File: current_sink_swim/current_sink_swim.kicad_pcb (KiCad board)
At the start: 2 copper layers, 22 parts, among them J1 Conn_01x02_Socket, J2 Conn_01x03_Socket, J3 Conn_01x02_Socket, Q1 BUK9575, U1 LMV358, U3 TC1016

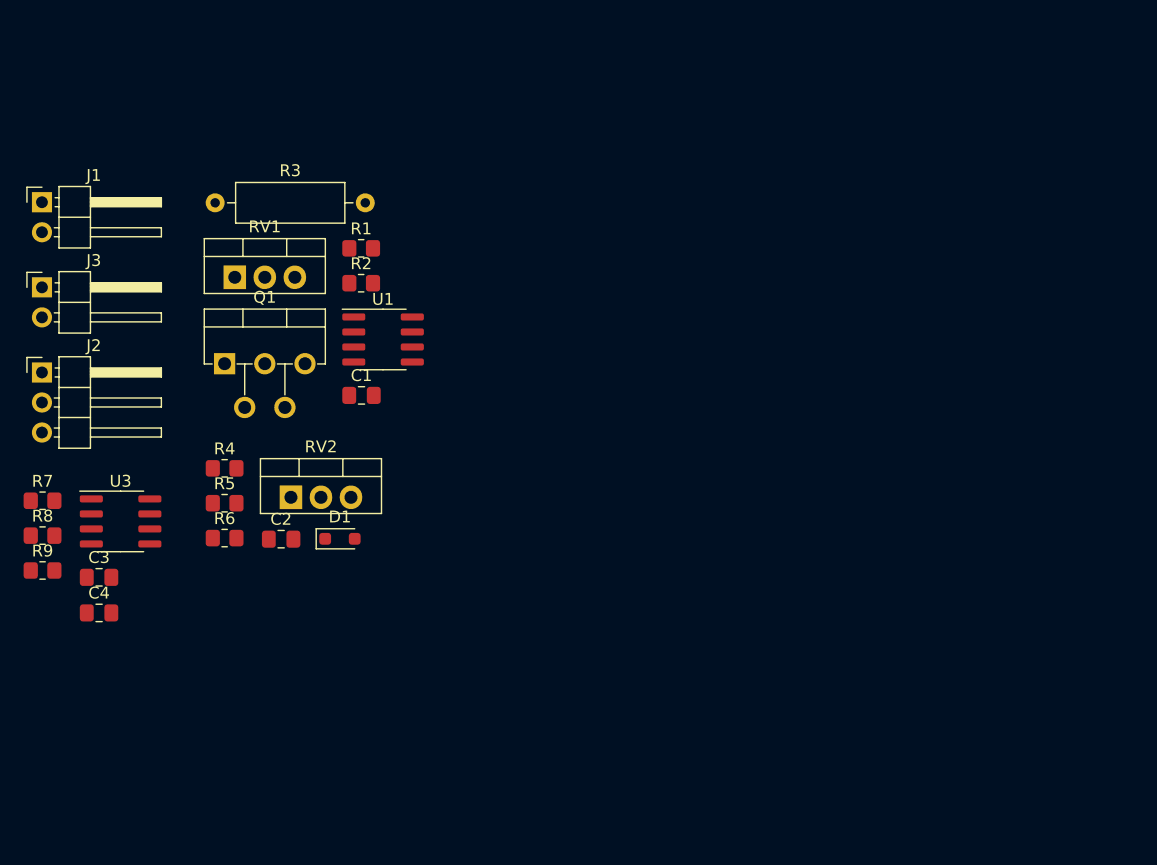
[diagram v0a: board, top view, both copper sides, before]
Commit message: created a rough board outline
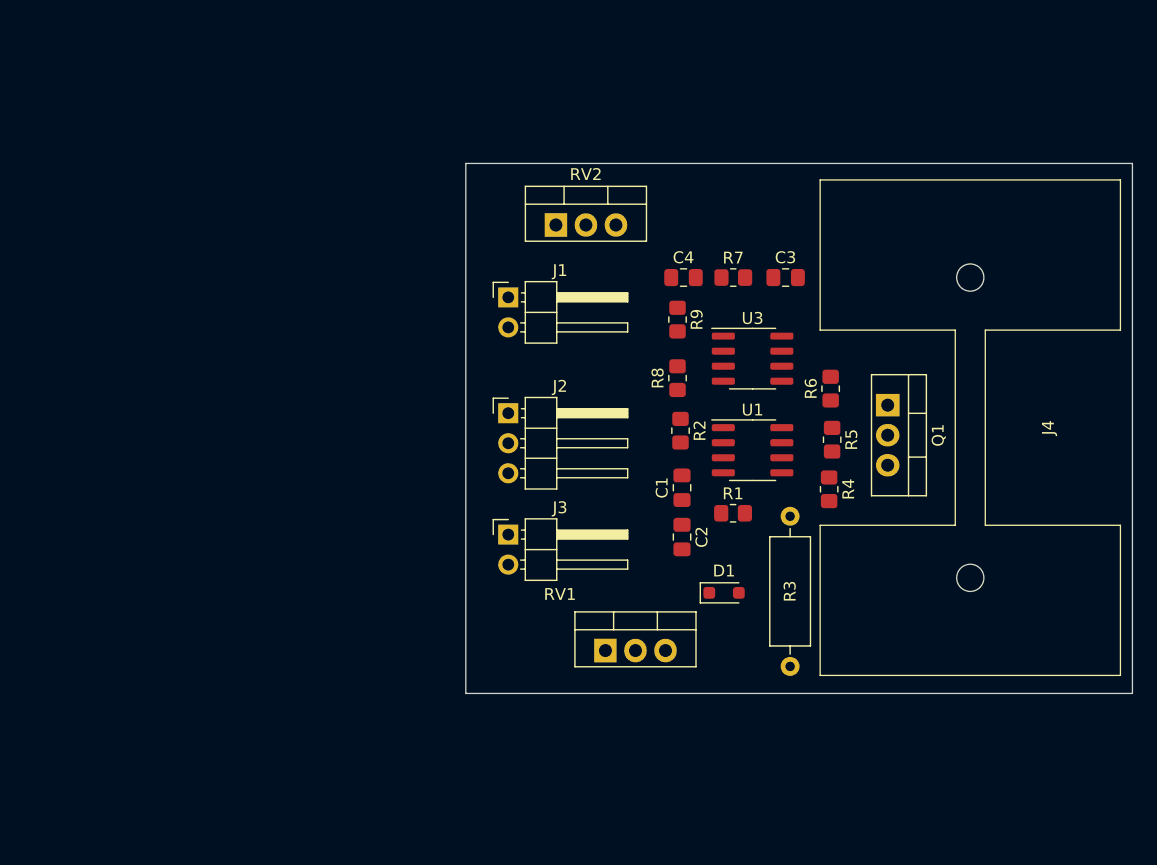
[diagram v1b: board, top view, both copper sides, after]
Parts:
- added J4: Conn_01x01_Pin, custom_modules:FAT-220, F.Cu at (142.5, 50.2)
- Q1: value BUK9575 -> IRF530NPBF; footprint Package_TO_SOT_THT:TO-220-5_P3.4x3.7mm_StaggerEven_Lead3.8mm_Vertical -> Package_TO_SOT_THT:TO-220-3_Vertical
- moved C3 63.4 mm to (126.9, 37.5)
- moved R7 61.4 mm to (122.4, 37.5)
- moved R9 57.8 mm to (117.7, 41.0), turned to -90 degrees
- moved C4 57.0 mm to (118.2, 37.5)
- moved Q1 56.2 mm to (135.5, 48.3), turned to -90 degrees
- moved R3 55.4 mm to (127.3, 57.7), turned to -90 degrees
- moved R8 55.3 mm to (117.7, 46.0), turned to 90 degrees
- moved U3 55.2 mm to (124.1, 44.3)
- moved R6 52.8 mm to (130.7, 46.9), turned to 90 degrees
- moved R5 51.7 mm to (130.8, 51.2), turned to -90 degrees
- moved R4 51.2 mm to (130.6, 55.4), turned to -90 degrees
- moved J3 44.6 mm to (103.4, 59.2)
- moved RV1 44.5 mm to (111.6, 69.0)
- moved J1 40.3 mm to (103.4, 39.1)
- moved J2 39.6 mm to (103.4, 48.9)
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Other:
- board outline added: 56.4 x 44.8 mm

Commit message: add correct pot symbols
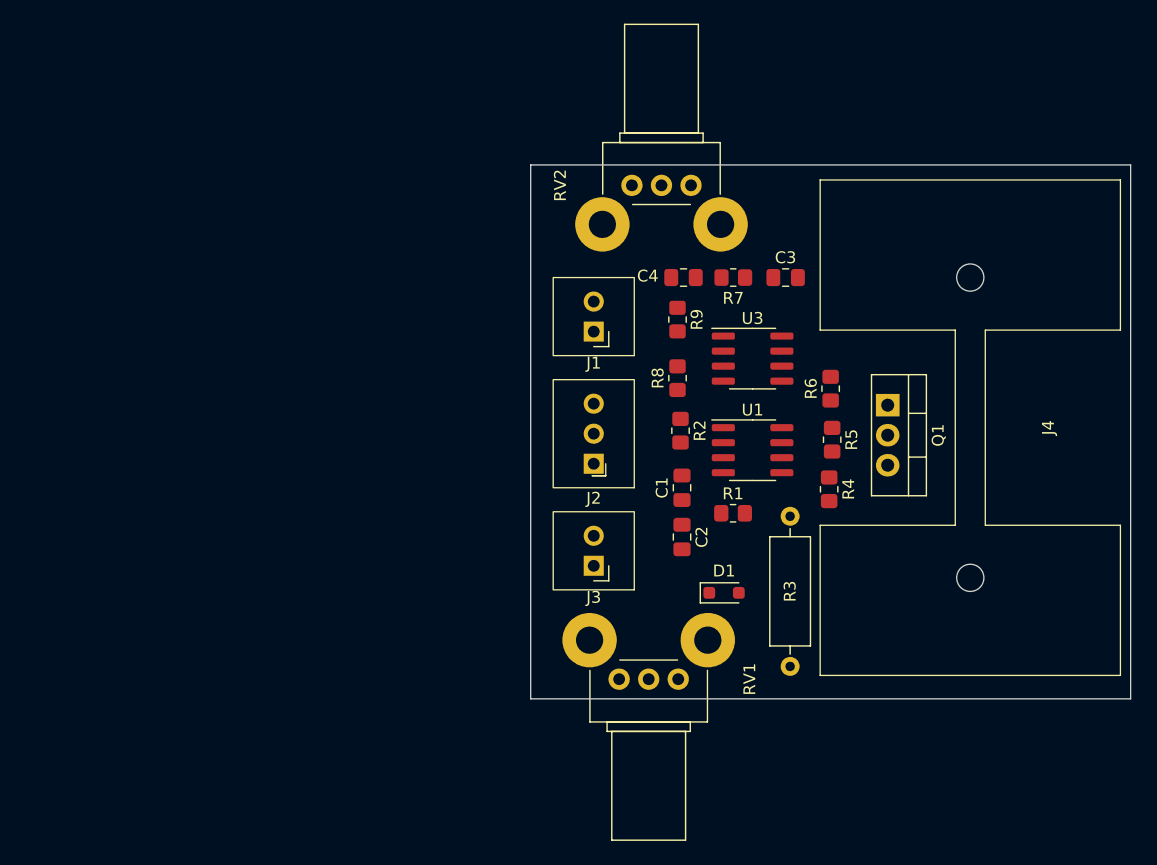
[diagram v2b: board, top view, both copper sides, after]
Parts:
- J1, J3: footprint Connector_PinHeader_2.54mm:PinHeader_1x02_P2.54mm_Horizontal -> custom_modules:te_2.54_2_pin_connector
- J2: footprint Connector_PinHeader_2.54mm:PinHeader_1x03_P2.54mm_Horizontal -> custom_modules:te_2.54mm_3_pin
- R1: value R -> 8.2k
- RV1, RV2: footprint Package_TO_SOT_THT:TO-220-3_Vertical -> Potentiometer_THT:Potentiometer_Bourns_PTV09A-2_Single_Horizontal
- moved RV2 11.9 mm to (118.9, 29.7), turned to 90 degrees
- moved J2 8.40 mm to (110.6, 53.2), turned to 180 degrees
- moved J1 7.79 mm to (110.6, 42.0), turned to 180 degrees
- moved J3 7.70 mm to (110.6, 61.8), turned to 180 degrees
- moved RV1 2.68 mm to (112.8, 71.4), turned to -90 degrees
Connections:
- R1 pad 1: Net-(U1A-+) -> 2.7V
- R1 pad 2: GND -> Net-(U1A-+)
- RV1 pad 2: 2.7V -> Net-(U1A-+)
- RV1 pad 3: Net-(U1A-+) -> GND
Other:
- board size 56.4 x 44.8 mm -> 50.7 x 45.2 mm

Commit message: update pcb layout with the new pot circuit
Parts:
- R1: value 8.2k -> 7.5k
- R4: value R -> 2.87k
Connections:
- R4 pad 1: Net-(U1B-+) -> 2.7V
- R4 pad 2: GND -> Net-(U1B-+)
- RV2 pad 2: 2.7V -> Net-(U1B-+)
- RV2 pad 3: Net-(U1B-+) -> GND
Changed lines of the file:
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@@
       (net 16 "unconnected-(RV2-Pad1)") (pinfunction "1") (pintype "passive"))
     (pad "2" thru_hole circle (at 0 -2.5 90) (size 1.8 1.8) (drill 1) (layers "*.Cu" "*.Mask")
-      (net 1 "2.7V") (pinfunction "2") (pintype "passive"))
+      (net 11 "Net-(U1B-+)") (pinfunction "2") (pintype "passive"))
     (pad "3" thru_hole circle (at 0 -5 90) (size 1.8 1.8) (drill 1) (layers "*.Cu" "*.Mask")
-      (net 11 "Net-(U1B-+)") (pinfunction "3") (pintype "passive"))
+      (net 2 "GND") (pinfunction "3") (pintype "passive"))
     (model "${KICAD6_3DMODEL_DIR}/Potentiometer_THT.3dshapes/Potentiometer_Bourns_PTV09A-2_Single_Horizontal.wrl"
       (offset (xyz 0 0 0))
@@
     (descr "Resistor SMD 0805 (2012 Metric), square (rectangular) end terminal, IPC_7351 nominal with elongated pad for handsoldering. (Body size source: IPC-SM-782 page 72, https://www.pcb-3d.com/wordpress/wp-content/uploads/ipc-sm-782a_amendment_1_and_2.pdf), generated with kicad-footprint-generator")
     (tags "resistor handsolder")
+    (property "MPN" "")
     (property "Sheetfile" "voltage_control.kicad_sch")
     (property "Sheetname" "Voltage Control")
@@
         (effects (font (size 1 1) (thickness 0.15)))
     )
-    (fp_text value "R" (at 0 1.65 90) (layer "F.Fab")
+    (fp_text value "2.87k" (at 0 1.65 90) (layer "F.Fab")
         (effects (font (size 1 1) (thickness 0.15)))
     )
@@
       (stroke (width 0.1) (type solid)) (layer "F.Fab"))
     (pad "1" smd roundrect (at -1 0 270) (size 1.2 1.4) (layers "F.Cu" "F.Paste" "F.Mask") (roundrect_rratio 0.208333)
+      (net 1 "2.7V") (pintype "passive"))
+    (pad "2" smd roundrect (at 1 0 270) (size 1.2 1.4) (layers "F.Cu" "F.Paste" "F.Mask") (roundrect_rratio 0.208333)
       (net 11 "Net-(U1B-+)") (pintype "passive"))
-    (pad "2" smd roundrect (at 1 0 270) (size 1.2 1.4) (layers "F.Cu" "F.Paste" "F.Mask") (roundrect_rratio 0.208333)
-      (net 2 "GND") (pintype "passive"))
     (model "${KICAD6_3DMODEL_DIR}/Resistor_SMD.3dshapes/R_0805_2012Metric.wrl"
       (offset (xyz 0 0 0))
@@
         (effects (font (size 1 1) (thickness 0.15)))
     )
-    (fp_text value "8.2k" (at 0 1.65) (layer "F.Fab")
-        (effects (font (size 1 1) (thickness 0.15)))
-    )
+    (fp_text value "7.5k" (at 0 1.65) (layer "F.Fab")
+        (effects (font (size 1 1) (thickness 0.15)))
+    )

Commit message: improve layout
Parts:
- C1, C2, C3, C4: moved to B.Cu
- moved D1 23.5 mm to (127.3, 41.3)
- moved C2 17.9 mm to (119.4, 41.6), turned to 0 degrees
- moved R4 17.8 mm to (119.4, 41.5), turned to 0 degrees
- moved R7 14.6 mm to (131.6, 48.9), turned to -90 degrees
- moved R9 14.3 mm to (126.3, 52.4), turned to 180 degrees
- moved R6 14.1 mm to (116.9, 44.0), turned to 180 degrees
- moved C4 11.7 mm to (125.5, 46.7), turned to 90 degrees
- moved R5 11.5 mm to (121.9, 44.0), turned to 180 degrees
- moved R8 10.4 mm to (127.9, 43.9), turned to 180 degrees
- moved C3 9.48 mm to (130.4, 46.3), turned to 180 degrees
- moved C1 8.83 mm to (119.2, 46.5), turned to 180 degrees
- moved RV1 7.33 mm to (119.4, 68.4)
- moved U1 7.21 mm to (118.1, 48.1)
- moved RV2 6.38 mm to (124.5, 32.7)
- moved U3 4.38 mm to (126.2, 48.2)
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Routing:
- added copper zone on B.Cu, net GND
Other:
- board size 50.7 x 45.2 mm -> 48.6 x 42.5 mm

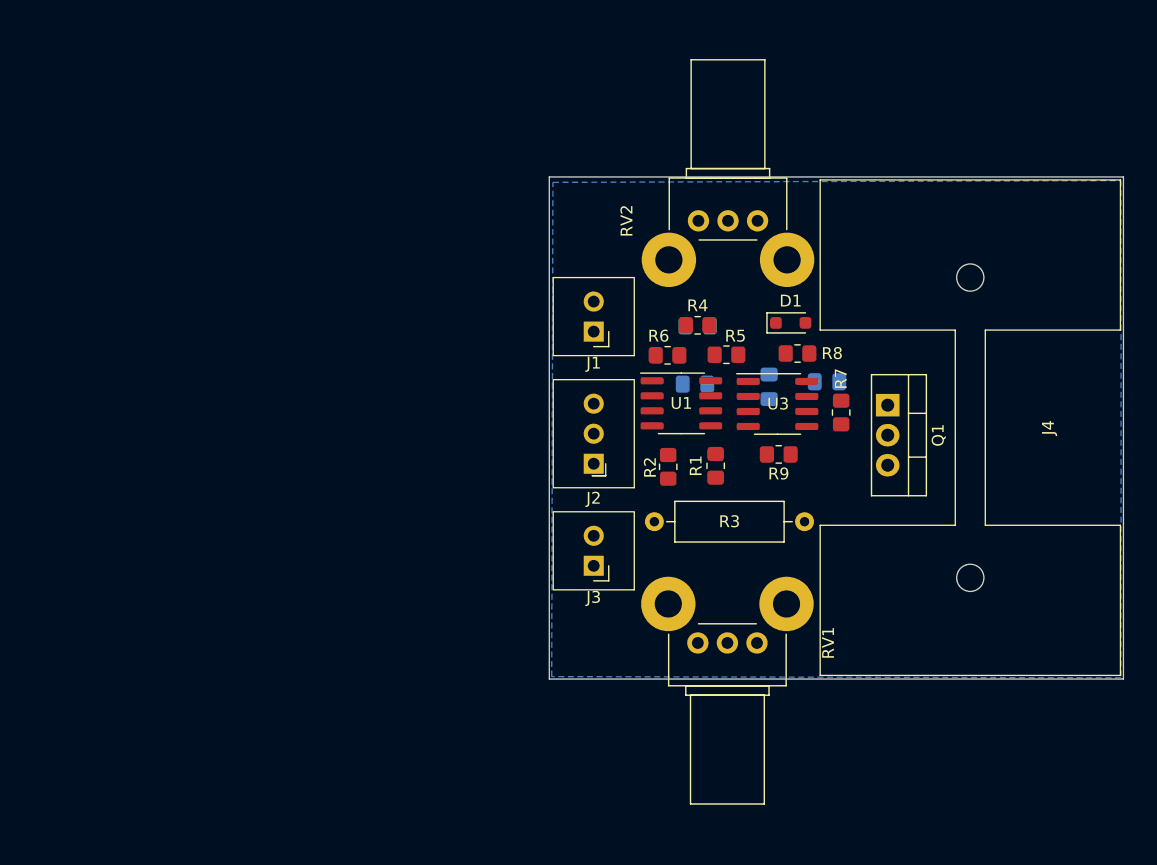
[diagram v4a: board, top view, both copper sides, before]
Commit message: first attempt at layout. Probably will be ripped up
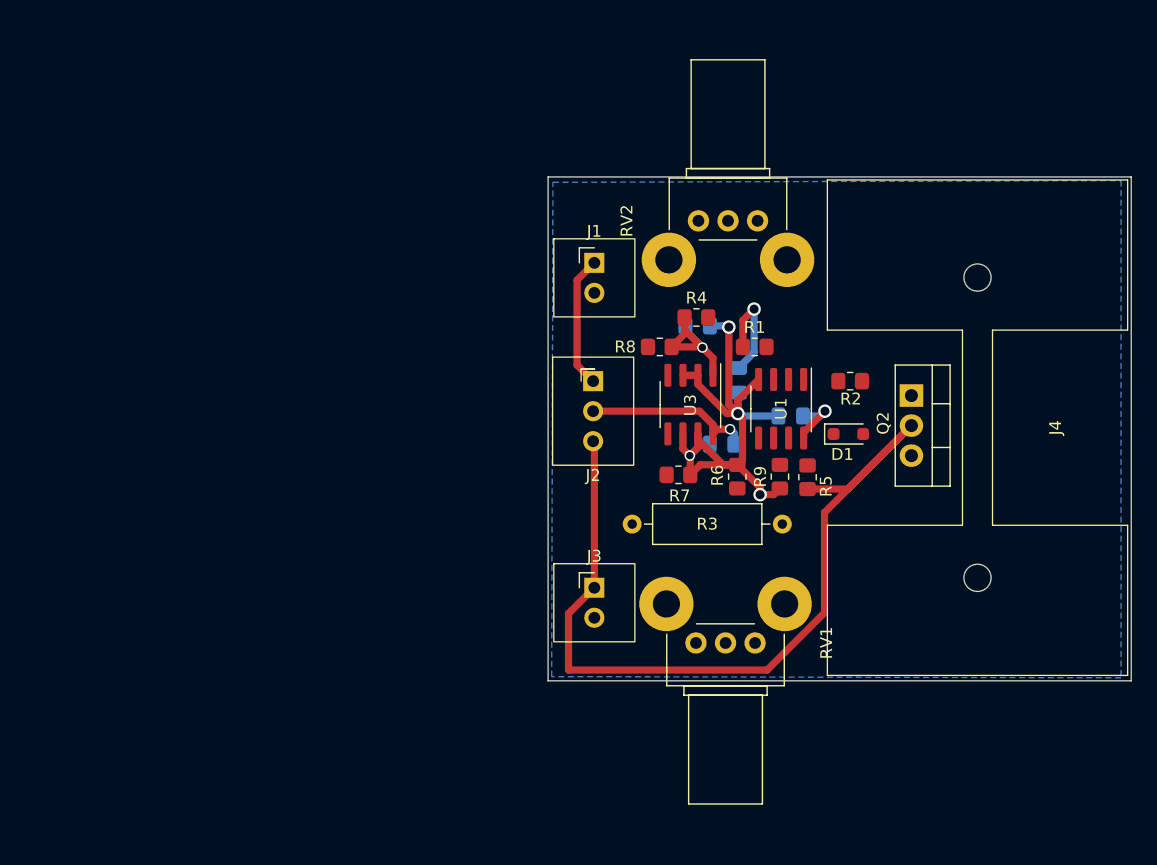
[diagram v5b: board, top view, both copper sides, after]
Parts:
- removed Q1: IRF530NPBF, Package_TO_SOT_THT:TO-220-3_Vertical
- added Q2: IRF540N, Package_TO_SOT_THT:TO-220-3_Vertical, F.Cu at (137.5, 47.4)
- moved R2 17.0 mm to (132.3, 46.2), turned to 0 degrees
- moved R7 14.7 mm to (117.8, 54.2), turned to 180 degrees
- moved R5 12.4 mm to (128.7, 54.4), turned to 90 degrees
- moved R6 11.8 mm to (122.8, 54.3), turned to 90 degrees
- moved R8 11.7 mm to (116.2, 43.3), turned to 0 degrees
- moved D1 10.6 mm to (132.2, 50.7)
- moved R1 10.6 mm to (124.3, 43.3), turned to 0 degrees
- moved C3 10.3 mm to (121.5, 51.6), turned to 0 degrees
- moved C1 8.53 mm to (127.3, 49.2)
- moved U1 8.45 mm to (126.5, 48.6), turned to -90 degrees
- moved U3 7.37 mm to (118.8, 48.2), turned to -90 degrees
- moved J2 6.99 mm to (110.6, 46.2), turned to 0 degrees
- moved J1 5.82 mm to (110.7, 36.2), turned to 0 degrees
- moved C4 2.65 mm to (122.9, 46.2)
- moved R3 1.89 mm to (126.6, 58.3)
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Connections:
- net / Current Control/FETDrain renamed Current_Sink+
- net /Power regulation/Vin renamed Vin
- net GND renamed Current_Sink-
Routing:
- net Current_Sink+: track 0.00 -> 73.9 mm
- net Current_Sink-: track 0.00 -> 51.5 mm, vias 0 -> 4
- net 2.7V: track 0.00 -> 28.1 mm, vias 0 -> 3
- net Vin: track 0.00 -> 14.4 mm, vias 0 -> 1
- net Net-(J1-Pin_1): track 0.00 -> 11.2 mm
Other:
- board size 48.6 x 42.5 mm -> 49.3 x 42.6 mm
